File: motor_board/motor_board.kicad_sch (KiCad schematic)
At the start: 30 parts, among them J1 Conn_01x05_Female, J3 Conn_01x06_Male, J4 Conn_01x06_Male, J7 Conn_01x06_Male, J8 Conn_01x06_Male, SW1 SW_Push, U1 ATmega32U4-A, U2 DRV8833PW, U4 DRV8833PW, Y1 Crystal_GND24

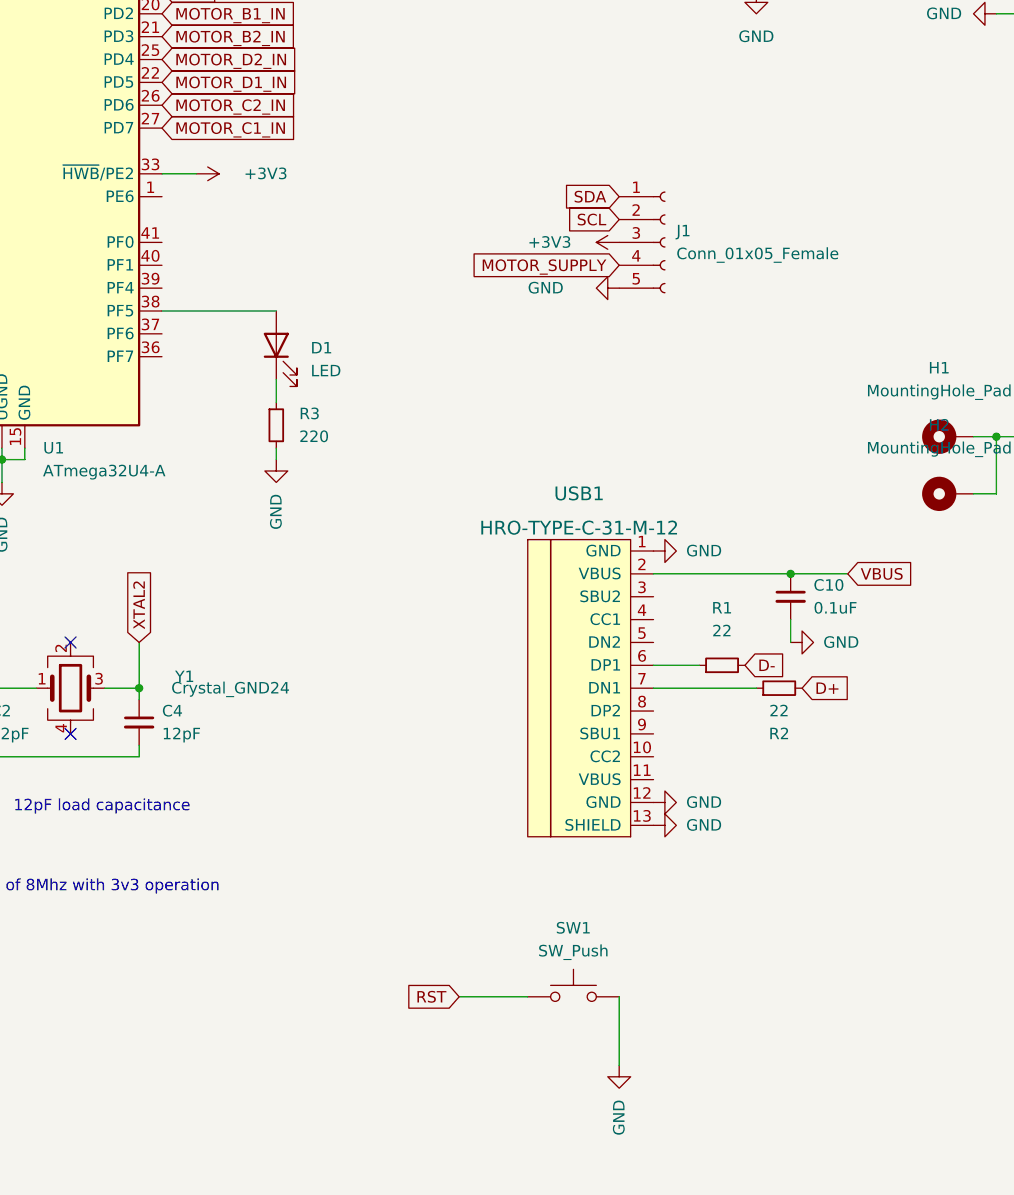
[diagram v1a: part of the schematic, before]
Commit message: Recent JLC order for motor controllers
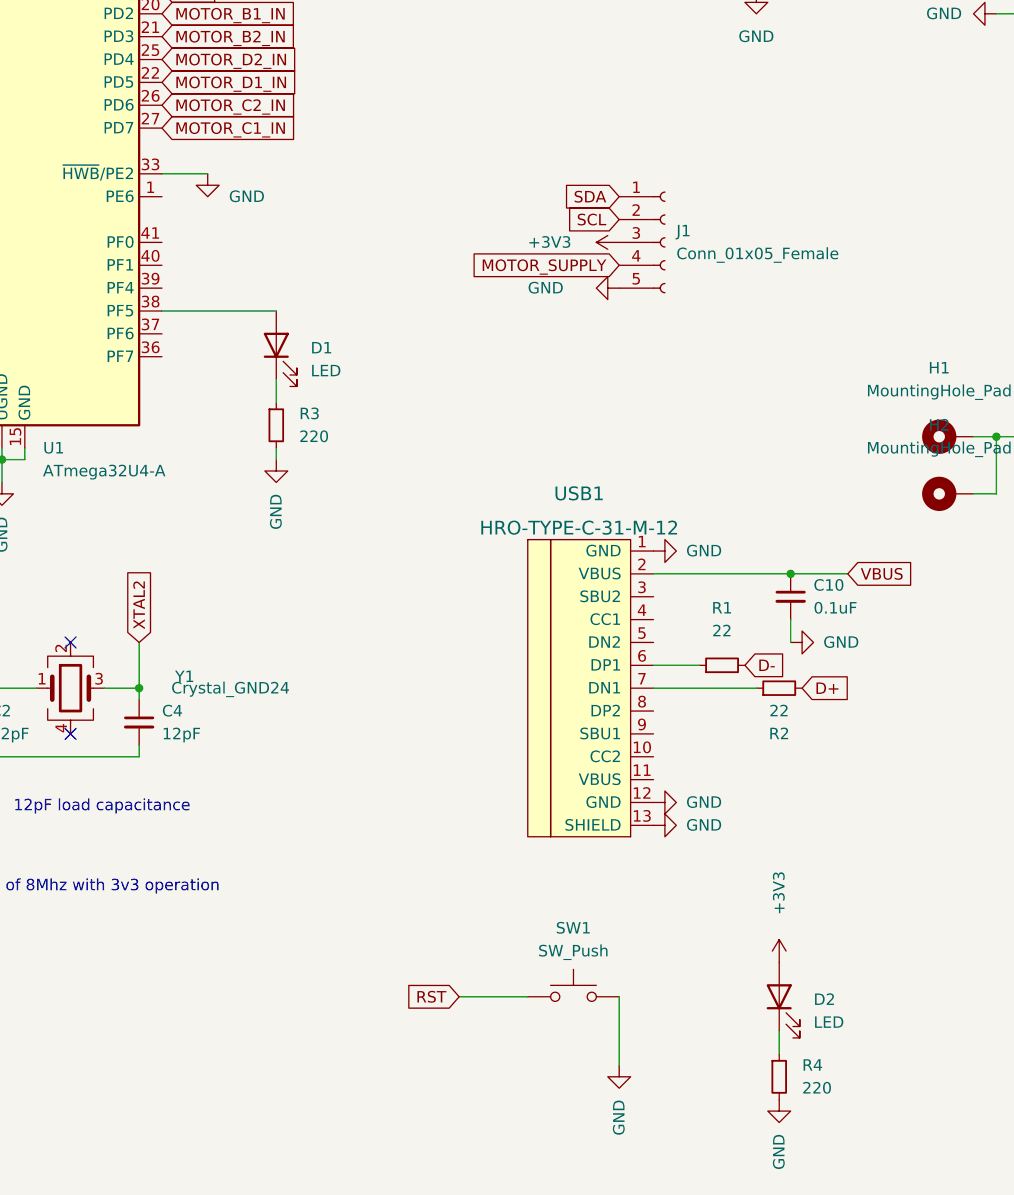
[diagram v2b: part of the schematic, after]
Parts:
- added D2: LED, LED_SMD:LED_0402_1005Metric, symbol Device:LED
- added R4: 220, Resistor_SMD:R_0402_1005Metric, symbol Device:R_Small
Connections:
- net +3V3: now also D2.2 (A); no longer U1.33 (~{HWB}/PE2)
- net GND: now also U1.33 (~{HWB}/PE2), R4.2
- new net: D2.1 (K), R4.1
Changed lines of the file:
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@@
+    (stroke (width 0) (type default) (color 0 0 0 0))
+  )
+  (wire (pts (xy 67.31 85.09) (xy 72.39 85.09))
     (stroke (width 0) (type default) (color 0 0 0 0))
   )
@@
     (stroke (width 0) (type default) (color 0 0 0 0))
   )
-  (wire (pts (xy 67.31 85.09) (xy 71.12 85.09))
-    (stroke (width 0) (type default) (color 0 0 0 0))
-  )
   (wire (pts (xy 45.72 148.59) (xy 45.72 149.86))
     (stroke (width 0) (type default) (color 0 0 0 0))
@@
   )
   (wire (pts (xy 200.66 30.48) (xy 200.66 34.29))
+    (stroke (width 0) (type default) (color 0 0 0 0))
+  )
+  (wire (pts (xy 135.89 180.34) (xy 135.89 182.88))
     (stroke (width 0) (type default) (color 0 0 0 0))
   )
@@
     (pin "1")
   )
+  (symbol (lib_id "Device:R_Small") (at 135.89 185.42 0) (unit 1)
+    (in_bom yes) (on_board yes) (fields_autoplaced)
+    (property "Reference" "R4" (id 0) (at 138.43 184.1499 0)
+      (effects (font (size 1.27 1.27)) (justify left))
+    )
+    (property "Value" "220" (id 1) (at 138.43 186.6899 0)
+      (effects (font (size 1.27 1.27)) (justify left))
+    )
+    (property "Footprint" "Resistor_SMD:R_0402_1005Metric" (id 2) (at 135.89 185.42 0)
+      (effects (font (size 1.27 1.27)) hide)
+    )
+    (property "Datasheet" "~" (id 3) (at 135.89 185.42 0)
+      (effects (font (size 1.27 1.27)) hide)
+    )
+    (property "LCSC" "C881401" (id 4) (at 135.89 185.42 0)
+      (effects (font (size 1.27 1.27)) hide)
+    )
+    (pin "1")
+    (pin "2")
+  )
   (symbol (lib_id "Device:C_Small") (at 27.94 67.31 0) (unit 1)
     (in_bom yes) (on_board yes) (fields_autoplaced)
@@
     )
     (property "Datasheet" "" (id 3) (at 262.89 67.31 0)
+      (effects (font (size 1.27 1.27)) hide)
+    )
+    (pin "1")
+  )
+  (symbol (lib_id "power:+3V3") (at 135.89 172.72 0) (unit 1)
+    (in_bom yes) (on_board yes)
+    (property "Reference" "#PWR0138" (id 0) (at 135.89 176.53 0)
+      (effects (font (size 1.27 1.27)) hide)
+    )
+    (property "Value" "+3V3" (id 1) (at 135.89 162.56 90)
+      (effects (font (size 1.27 1.27)) (justify right))
+    )
+    (property "Footprint" "" (id 2) (at 135.89 172.72 0)
+      (effects (font (size 1.27 1.27)) hide)
+    )
+    (property "Datasheet" "" (id 3) (at 135.89 172.72 0)
       (effects (font (size 1.27 1.27)) hide)
     )
@@
     (pin "2")
   )
-  (symbol (lib_id "power:+3V3") (at 71.12 85.09 270) (unit 1)
-    (in_bom yes) (on_board yes)
-    (property "Reference" "#PWR0135" (id 0) (at 67.31 85.09 0)
-      (effects (font (size 1.27 1.27)) hide)
-    )
-    (property "Value" "+3V3" (id 1) (at 81.28 85.09 90)
-      (effects (font (size 1.27 1.27)) (justify right))
-    )
-    (property "Footprint" "" (id 2) (at 71.12 85.09 0)
-      (effects (font (size 1.27 1.27)) hide)
-    )
-    (property "Datasheet" "" (id 3) (at 71.12 85.09 0)
-      (effects (font (size 1.27 1.27)) hide)
-    )
-    (pin "1")
-  )
   (symbol (lib_id "power:GND") (at 162.56 114.3 90) (unit 1)
     (in_bom yes) (on_board yes)
@@
     )
     (pin "1")
+  )
+  (symbol (lib_id "Device:LED") (at 135.89 176.53 90) (unit 1)
+    (in_bom yes) (on_board yes) (fields_autoplaced)
+    (property "Reference" "D2" (id 0) (at 139.7 176.8474 90)
+      (effects (font (size 1.27 1.27)) (justify right))
+    )
+    (property "Value" "LED" (id 1) (at 139.7 179.3874 90)
+      (effects (font (size 1.27 1.27)) (justify right))
+    )
+    (property "Footprint" "LED_SMD:LED_0402_1005Metric" (id 2) (at 135.89 176.53 0)
+      (effects (font (size 1.27 1.27)) hide)
+    )
+    (property "Datasheet" "~" (id 3) (at 135.89 176.53 0)
+      (effects (font (size 1.27 1.27)) hide)
+    )
+    (property "LCSC" "C273598" (id 4) (at 135.89 176.53 0)
+      (effects (font (size 1.27 1.27)) hide)
+    )
+    (pin "1")
+    (pin "2")
   )
   (symbol (lib_id "Mechanical:MountingHole_Pad") (at 154.94 120.65 90) (unit 1)
@@
     (pin "1")
   )
+  (symbol (lib_id "power:GND") (at 72.39 85.09 0) (unit 1)
+    (in_bom yes) (on_board yes)
+    (property "Reference" "#PWR0135" (id 0) (at 72.39 91.44 0)
+      (effects (font (size 1.27 1.27)) hide)
+    )
+    (property "Value" "GND" (id 1) (at 78.74 87.63 0)
+      (effects (font (size 1.27 1.27)) (justify right))
+    )
+    (property "Footprint" "" (id 2) (at 72.39 85.09 0)
+      (effects (font (size 1.27 1.27)) hide)
+    )
+    (property "Datasheet" "" (id 3) (at 72.39 85.09 0)
+      (effects (font (size 1.27 1.27)) hide)
+    )
+    (pin "1")
+  )
+  (symbol (lib_id "power:GND") (at 135.89 187.96 0) (unit 1)
+    (in_bom yes) (on_board yes)
+    (property "Reference" "#PWR0139" (id 0) (at 135.89 194.31 0)
+      (effects (font (size 1.27 1.27)) hide)
+    )
+    (property "Value" "GND" (id 1) (at 135.89 191.77 90)
+      (effects (font (size 1.27 1.27)) (justify right))
+    )
+    (property "Footprint" "" (id 2) (at 135.89 187.96 0)
+      (effects (font (size 1.27 1.27)) hide)
+    )
+    (property "Datasheet" "" (id 3) (at 135.89 187.96 0)
+      (effects (font (size 1.27 1.27)) hide)
+    )
+    (pin "1")
+  )
   (symbol (lib_id "power:GND") (at 175.26 39.37 270) (unit 1)
     (in_bom yes) (on_board yes)
@@
       (reference "#PWR0134") (unit 1) (value "GND") (footprint "")
     )
-    (path "/28fc3dc5-1160-4903-9b5d-aec365a516e4"
-      (reference "#PWR0135") (unit 1) (value "+3V3") (footprint "")
+    (path "/cc4b7075-9d4b-4099-bea5-376e5edd14dc"
+      (reference "#PWR0135") (unit 1) (value "GND") (footprint "")
     )
     (path "/047abcff-0f7e-40e1-86b2-02cf58ac7b36"
@@
       (reference "#PWR0137") (unit 1) (value "GND") (footprint "")
     )
+    (path "/254fc27e-1633-4dad-a4b2-4a2750929be7"
+      (reference "#PWR0138") (unit 1) (value "+3V3") (footprint "")
+    )
+    (path "/d3117549-10fe-4839-8065-05e2c4e04536"
+      (reference "#PWR0139") (unit 1) (value "GND") (footprint "")
+    )
     (path "/73dd0ac9-8faf-4b19-b289-835271bd4d8c"
       (reference "C1") (unit 1) (value "1uF") (footprint "Capacitor_SMD:C_0402_1005Metric")
@@
       (reference "D1") (unit 1) (value "LED") (footprint "LED_SMD:LED_0402_1005Metric")
     )
+    (path "/2c2c2a1f-1896-4083-a3ed-51f88a024129"
+      (reference "D2") (unit 1) (value "LED") (footprint "LED_SMD:LED_0402_1005Metric")
+    )
     (path "/01f18b55-48d6-4a40-88ea-e5978dc6c964"
       (reference "H1") (unit 1) (value "MountingHole_Pad") (footprint "MountingHole:MountingHole_2.2mm_M2_DIN965_Pad")
@@
       (reference "R3") (unit 1) (value "220") (footprint "Resistor_SMD:R_0402_1005Metric")
     )
+    (path "/12d92fbe-6376-409f-8e2e-9c5d66149852"
+      (reference "R4") (unit 1) (value "220") (footprint "Resistor_SMD:R_0402_1005Metric")
+    )
     (path "/46278e04-9314-456c-b22e-af6f45f15026"
